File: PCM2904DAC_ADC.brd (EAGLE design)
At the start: 85 x 56 mm, 48 parts, among them IC1 LM358D, Q1 12MHz, X1 V+, D-, D+, GND

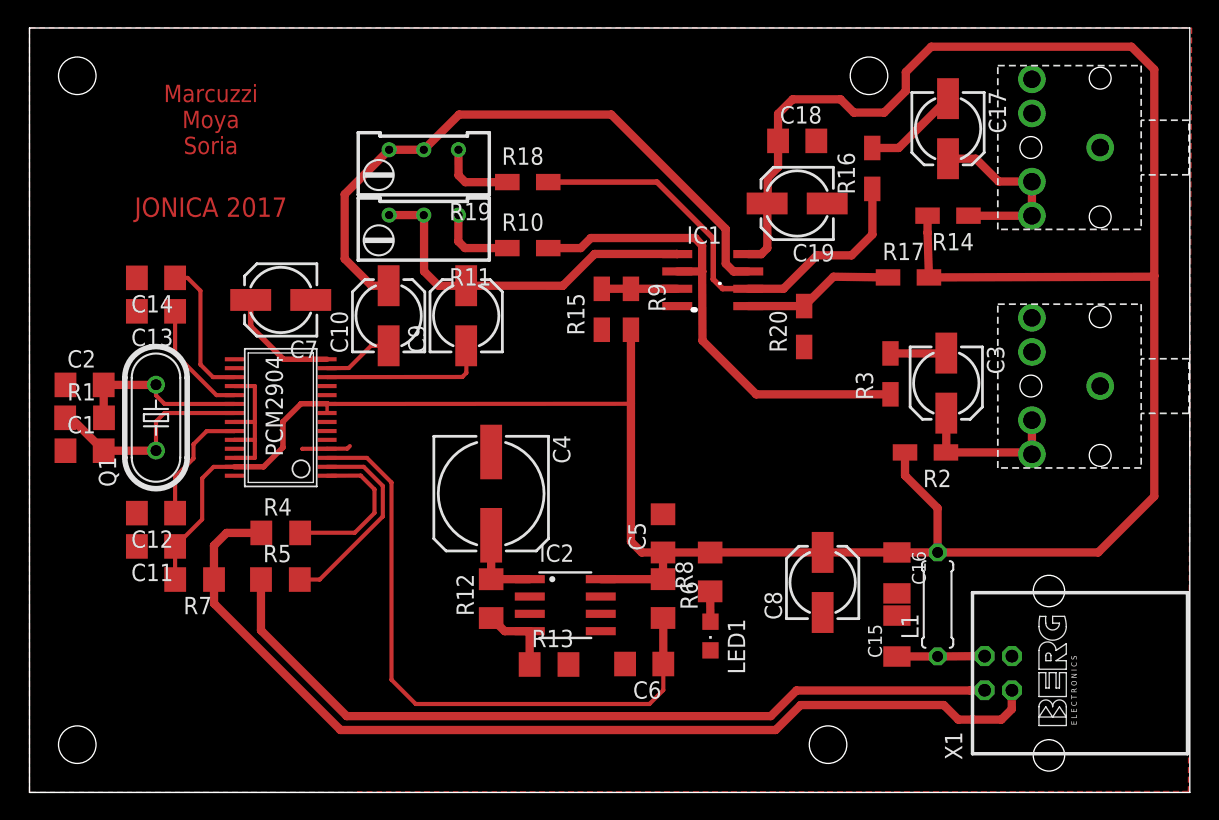
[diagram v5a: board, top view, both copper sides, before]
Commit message: Pasado todo a la capa bottom.
No le cambié el usb porque había que rediseñar la pcb y ando con poco
tiempo, si quieren lo vemos dps!

Salu2
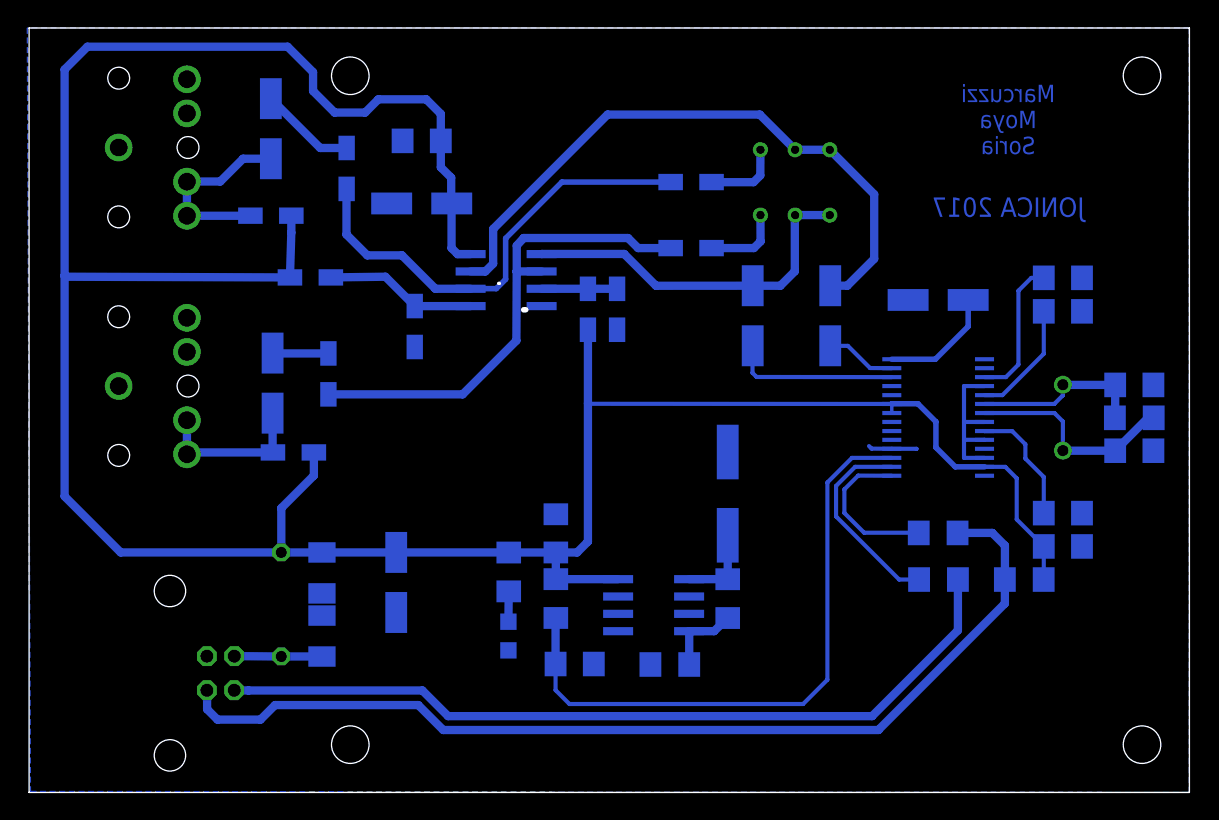
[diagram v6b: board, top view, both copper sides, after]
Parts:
- moved C1 76.9 mm to (80.9, 25.0), flipped to the bottom
- moved C2 76.9 mm to (80.9, 29.9), flipped to the bottom
- moved R1 76.9 mm to (80.9, 27.4), flipped to the bottom
- moved U$1 71.9 mm to (6.53, 47.2), flipped to the bottom
- moved U$8 71.9 mm to (6.53, 29.8), flipped to the bottom
- moved C11 66.4 mm to (75.7, 18.0), flipped to the bottom
- moved C12 66.4 mm to (75.7, 20.5), flipped to the bottom
- moved C13 66.4 mm to (75.7, 35.2), flipped to the bottom
- moved C14 66.4 mm to (75.7, 37.7), flipped to the bottom
- moved Q1 66.4 mm to (75.7, 27.5), flipped to the bottom
- moved X1 64.4 mm to (10.3, 8.74), flipped to the bottom
- moved R7 60.8 mm to (72.9, 15.6), flipped to the bottom
- moved C17 49.6 mm to (17.7, 48.6), flipped to the bottom
- moved R14 49.6 mm to (17.7, 42.3), flipped to the bottom
- moved C3 49.4 mm to (17.8, 30.0), flipped to the bottom
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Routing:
- added copper zone on layer 16, net GND
- removed copper zone on layer 1, net GND
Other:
- outline, holes or cut-outs redrawn

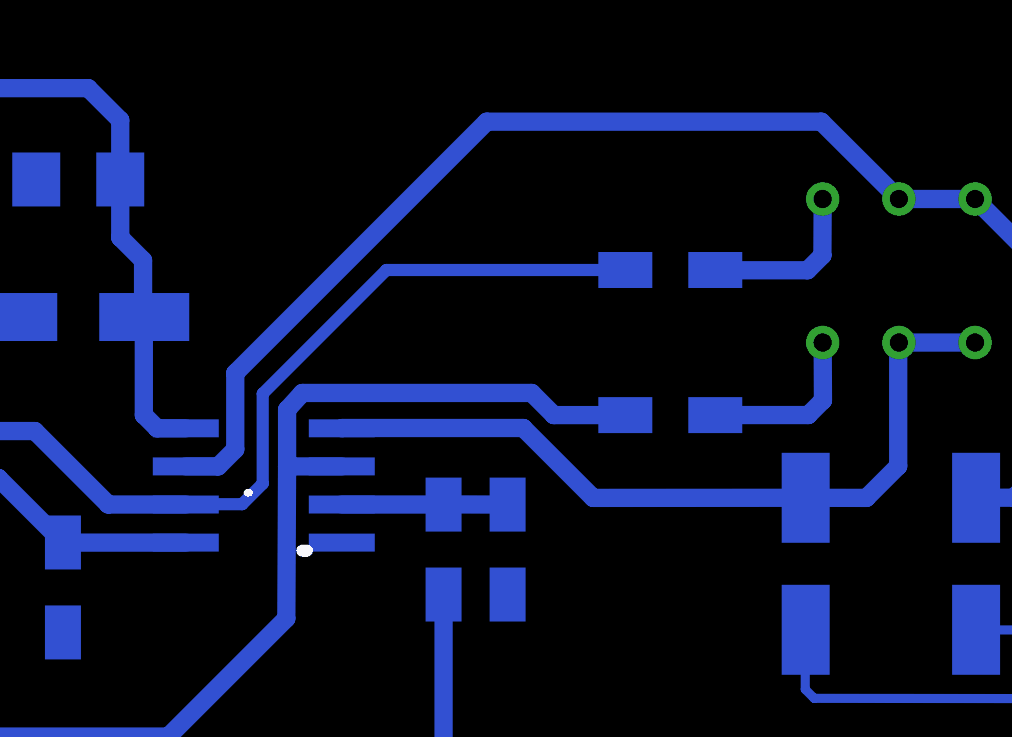
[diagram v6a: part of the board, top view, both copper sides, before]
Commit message: Modificada posicion de un cap
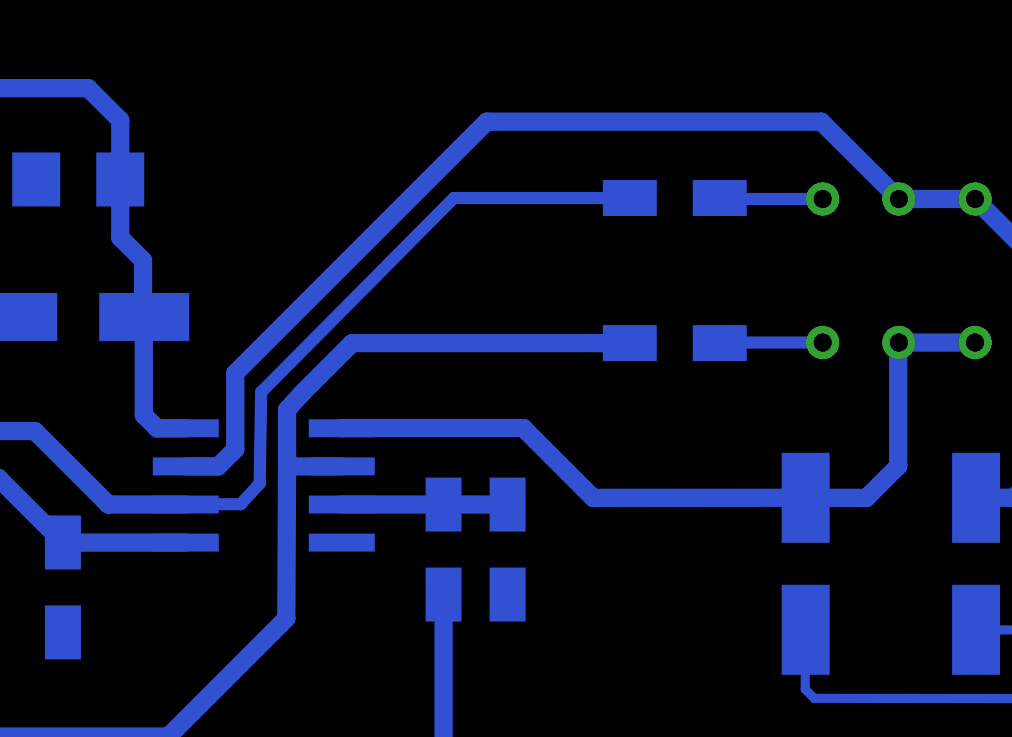
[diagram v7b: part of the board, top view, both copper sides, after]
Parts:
- moved R10 2.40 mm to (48.6, 42.3)
- moved R18 2.40 mm to (48.6, 47.1)
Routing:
- net N$17: track 5.73 -> 3.44 mm
- net N$12: track 5.66 -> 3.44 mm
- net N$10: track 33.9 -> 35.0 mm
- net N$15: track 36.0 -> 36.5 mm
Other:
- outline, holes or cut-outs redrawn
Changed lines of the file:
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@@
 <setting verticaltext="up"/>
 </settings>
-<grid distance="0.1" unitdist="mm" unit="mm" style="lines" multiple="1" display="yes" altdistance="5" altunitdist="mil" altunit="mil"/>
+<grid distance="1" unitdist="mil" unit="mil" style="lines" multiple="1" display="yes" altdistance="5" altunitdist="mil" altunit="mil"/>
 <layers>
 <layer number="1" name="Top" color="4" fill="1" visible="yes" active="yes"/>
@@
 <hole x="81.5" y="52.5" drill="2.75"/>
 <hole x="23.5" y="52.5" drill="2.75"/>
-<wire x1="36.3532" y1="35.3568" x2="36.2008" y2="35.3568" width="0.4064" layer="20"/>
-<wire x1="34.4228" y1="37.2872" x2="34.372" y2="37.2872" width="0.254" layer="20"/>
 <text x="71.6846" y="49.3014" size="1.27" layer="16" font="vector" rot="MR0" align="center">Marcuzzi
 Moya
@@
 <element name="R3" library="rcl" library_urn="urn:adsk.eagle:library:334" package="R1206W" package3d_urn="urn:adsk.eagle:package:23539/1" value="" x="21.8966" y="30.66026875" rot="MR90"/>
 <element name="R9" library="rcl" library_urn="urn:adsk.eagle:library:334" package="R1206W" package3d_urn="urn:adsk.eagle:package:23539/1" value="" x="40.909" y="35.39425" rot="MR270"/>
-<element name="R10" library="rcl" library_urn="urn:adsk.eagle:library:334" package="R1206W" package3d_urn="urn:adsk.eagle:package:23539/1" value="" x="48.4663" y="39.8763" rot="MR0"/>
+<element name="R10" library="rcl" library_urn="urn:adsk.eagle:library:334" package="R1206W" package3d_urn="urn:adsk.eagle:package:23539/1" value="" x="48.6163" y="42.2763" rot="MR0"/>
 <element name="R11" library="rcl" library_urn="urn:adsk.eagle:library:334" package="RTRIM64W" package3d_urn="urn:adsk.eagle:package:23748/1" value="" x="56.08605" y="41.0249" rot="MR90"/>
 <element name="C3" library="rcl" package="153CLV-0505" value="" x="17.80873125" y="29.9852" rot="MR270"/>
@@
 <element name="R16" library="rcl" library_urn="urn:adsk.eagle:library:334" package="R1206W" package3d_urn="urn:adsk.eagle:package:23539/1" value="" x="23.2324" y="45.7116" rot="MR90"/>
 <element name="R17" library="rcl" library_urn="urn:adsk.eagle:library:334" package="R1206W" package3d_urn="urn:adsk.eagle:package:23539/1" value="" x="20.5775" y="37.728" rot="MR0"/>
-<element name="R18" library="rcl" library_urn="urn:adsk.eagle:library:334" package="R1206W" package3d_urn="urn:adsk.eagle:package:23539/1" value="" x="48.4663" y="44.713" rot="MR0"/>
+<element name="R18" library="rcl" library_urn="urn:adsk.eagle:library:334" package="R1206W" package3d_urn="urn:adsk.eagle:package:23539/1" value="" x="48.6163" y="47.113" rot="MR0"/>
 <element name="R19" library="rcl" library_urn="urn:adsk.eagle:library:334" package="RTRIM64W" package3d_urn="urn:adsk.eagle:package:23748/1" value="" x="56.08605" y="45.8098" rot="MR90"/>
 <element name="C17" library="rcl" package="153CLV-0505" value="" x="17.68173125" y="48.6238" rot="MR270"/>
@@
 <contactref element="R3" pad="1"/>
 <contactref element="R10" pad="2"/>
-<wire x1="46.9673" y1="39.8763" x2="44.5845" y2="39.8763" width="0.6096" layer="16"/>
-<wire x1="44.5845" y1="39.8763" x2="43.8462" y2="40.6146" width="0.6096" layer="16"/>
-<wire x1="36.2008" y1="40.6146" x2="43.8462" y2="40.6146" width="0.6096" layer="16"/>
 <wire x1="35.6928" y1="38.1661" x2="35.6928" y2="40.0558" width="0.6096" layer="16"/>
 <wire x1="35.6928" y1="40.0558" x2="36.2008" y2="40.6146" width="0.6096" layer="16"/>
@@
 <wire x1="21.8966" y1="29.16126875" x2="31.73246875" y2="29.16126875" width="0.6096" layer="16"/>
 <wire x1="31.73246875" y1="29.16126875" x2="35.6674" y2="33.0962" width="0.6096" layer="16"/>
+<wire x1="36.2008" y1="40.6146" x2="37.8625" y2="42.2763" width="0.6096" layer="16"/>
+<wire x1="37.8625" y1="42.2763" x2="47.1173" y2="42.2763" width="0.6096" layer="16"/>
 </signal>
 <signal name="N$17">
 <contactref element="R11" pad="1"/>
 <contactref element="R10" pad="1"/>
-<wire x1="53.54605" y1="42.2949" x2="53.5553" y2="40.3669" width="0.6096" layer="16"/>
-<wire x1="53.5553" y1="40.3669" x2="53.0664" y2="39.878" width="0.6096" layer="16"/>
-<wire x1="53.0664" y1="39.878" x2="49.9623" y2="39.878" width="0.6096" layer="16"/>
-<wire x1="49.9623" y1="39.878" x2="49.9653" y2="39.8763" width="0.6096" layer="16"/>
+<wire x1="50.1153" y1="42.2763" x2="50.1339" y2="42.2949" width="0.4064" layer="16"/>
+<wire x1="50.1339" y1="42.2949" x2="53.54605" y2="42.2949" width="0.4064" layer="16"/>
 </signal>
 <signal name="N$18">
@@
 <contactref element="IC1" pad="6"/>
 <wire x1="32.3164" y1="37.0332" x2="32.3164" y2="36.8961" width="0.254" layer="16"/>
-<wire x1="46.9673" y1="44.713" x2="39.0038" y2="44.713" width="0.4064" layer="16"/>
-<wire x1="39.0038" y1="44.713" x2="34.88" y2="40.5892" width="0.4064" layer="16"/>
-<wire x1="34.88" y1="40.5892" x2="34.88" y2="37.592" width="0.4064" layer="16"/>
-<wire x1="34.88" y1="37.592" x2="34.1942" y2="36.9062" width="0.4064" layer="16"/>
-<wire x1="34.1942" y1="36.9062" x2="32.3265" y2="36.9062" width="0.4064" layer="16"/>
+<wire x1="34.7784" y1="37.592" x2="34.8292" y2="40.64" width="0.4064" layer="16"/>
+<wire x1="34.7784" y1="37.592" x2="34.1434" y2="36.9062" width="0.4064" layer="16"/>
+<wire x1="34.1434" y1="36.9062" x2="32.3265" y2="36.9062" width="0.4064" layer="16"/>
 <wire x1="32.3265" y1="36.9062" x2="32.3164" y2="36.8961" width="0.4064" layer="16"/>
 <wire x1="32.3164" y1="36.8961" x2="29.7339" y2="36.8961" width="0.6096" layer="16"/>
@@
 <wire x1="23.2214" y1="40.8686" x2="23.2214" y2="44.2016" width="0.6096" layer="16"/>
 <wire x1="23.2214" y1="44.2016" x2="23.2324" y2="44.2126" width="0.6096" layer="16"/>
+<wire x1="41.2514" y1="47.113" x2="47.1173" y2="47.113" width="0.4064" layer="16"/>
+<wire x1="34.8292" y1="40.64" x2="41.2514" y2="47.113" width="0.4064" layer="16"/>
 </signal>
 <signal name="N$12">
 <contactref element="R19" pad="1"/>
 <contactref element="R18" pad="1"/>
-<wire x1="53.54605" y1="47.0798" x2="53.5368" y2="45.1998" width="0.6096" layer="16"/>
-<wire x1="53.5368" y1="45.1998" x2="53.041" y2="44.704" width="0.6096" layer="16"/>
-<wire x1="53.041" y1="44.704" x2="49.979" y2="44.704" width="0.6096" layer="16"/>
-<wire x1="49.979" y1="44.704" x2="49.9653" y2="44.713" width="0.6096" layer="16"/>
+<wire x1="50.1153" y1="47.113" x2="50.1485" y2="47.0798" width="0.4064" layer="16"/>
+<wire x1="50.1485" y1="47.0798" x2="53.54605" y2="47.0798" width="0.4064" layer="16"/>
 </signal>
 <signal name="N$14">
